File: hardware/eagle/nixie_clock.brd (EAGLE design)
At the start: 199.4 x 199.4 mm, 81 parts, among them IC1 74141N, IC10 7477N, IC11 74141N, IC12 7477N, IC13 74HCT259N, IC15 7477N, IC2 7477N, IC3 74141N, IC4 7477N, IC5 74141N, IC6 7477N, IC7 74141N, IC8 7477N, IC9 74141N, J1 RASPBERRYPI-40-PIN-GPIO, J1_180V 22-27-2021-02, J1_5V1 22-27-2021-02, J1_5V2 22-27-2021-02, K1 4052, SW1 ROTARTY_ENCODER

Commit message: Updated eagle project
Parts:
- removed SV1, SV11, SV13, SV3, SV5, SV7, SV9: (no value), con-lstb:MA06-1
- added J10, J4, J5, J6, J7, J8, J9: (no value), SparkFun-Connectors:1X08_ROUND
- added J2: (no value), SparkFun-Connectors:AVR_ICSP
- added J3: (no value), SparkFun-Connectors:1X04
- added SV17: (no value), con-lstb:MA09-2
- SV10, SV12, SV14, SV2, SV4, SV6, SV8: device con-lstb:MA05-1 -> SparkFun-Connectors:1X07
- moved R12 130.8 mm to (3.81, 36.8), turned to 270 degrees
- moved D1 128.1 mm to (90.2, 95.2), turned to 0 degrees
- moved IN-8-1 128.1 mm to (90.2, 95.2)
- moved SV14 122.3 mm to (97.8, 105.4)
- moved J1 13.1 mm to (181.6, 47.0)
- moved SV8 7.62 mm to (108.0, 27.9)
- moved SV4 7.62 mm to (62.2, 27.9)
- moved SV2 6.35 mm to (40.6, 27.9)
- moved SV12 6.35 mm to (154.9, 27.9)
- moved SV6 6.35 mm to (86.4, 27.9)
- moved SV10 5.08 mm to (132.1, 27.9)
- moved R5 2.54 mm to (124.5, 2.54), turned to 180 degrees
- moved R3 1.27 mm to (78.7, 2.54), turned to 180 degrees
- moved R6 1.27 mm to (147.3, 2.54), turned to 180 degrees
- moved R1 1.27 mm to (33.0, 2.54), turned to 180 degrees
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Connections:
- removed net 3.3V: J1.1, J1.17
- removed net 5V: J1.2, J1.4
- new net BLUE: J3.3, R11.2, SV10.7, SV12.7, SV2.7, SV4.7, SV6.7, SV8.7
- new net GREEN: J3.2, R10.2, SV10.6, SV12.6, SV2.6, SV4.6, SV6.6, SV8.6
- new net GROUND: C1.2, C10.2, C11.2, C12.2, C13.2, C16.2, C17.2, C2.2, C3.2, C4.2, C5.2, C6.2, C7.2, C8.2, C9.2, D2.A, IC1.5, IC10.4, IC11.5, IC12.4, IC13.13, IC13.16, IC15.4, IC2.4, IC3.5, IC4.4, IC5.5, IC6.4, IC7.5, IC8.4, IC9.5, J1_5V1.2, J3.4, K1.2, R12.2, R7.2, R8.1, SV10.5, SV12.5, SV16.1, SV2.5, SV4.5, SV6.5, SV8.5, ULN1.10
- new net N$145: J1.1, J2.1, SV17.1
- new net N$150: J7.8, R4.1
- new net N$153: J1.4, J2.4, SV17.4
- new net N$154: J1.3, J2.3, SV17.3
- new net N$155: J1.5, J2.5, SV17.5
- new net N$156: J1.6, J2.6, J2.9, SV17.6
- new net N$157: J1.27, SV17.7
- new net N$158: J1.28, SV17.9
- new net N$159: J1.8, SV17.8
- new net N$160: J1.10, SV17.10
- new net N$161: J1.19, SV17.11
- new net N$162: J1.21, SV17.13
- new net N$163: J1.23, SV17.15
- new net N$164: J4.8, R1.1
- new net N$165: J1.9, SV17.12
- new net N$166: J1.24, SV17.14
- new net N$167: J1.26, SV17.16
- new net N$168: J1.14, SV17.18
- new net N$169: J6.8, R3.1
- new net N$170: R1.2, R2.2, R3.2, R4.2, R5.2, R6.2
- new net N$171: J5.8, R2.1
- new net N$172: J1.2, J2.2, SV17.2
- new net RED: J3.1, R9.2, SV10.4, SV12.4, SV2.4, SV4.4, SV6.4, SV8.4
- net GND: no longer J1.14, J1.6, J1.9
- net N$1: now also IN-8-1.4, J10.1; no longer R2.1, SV4.3
- net N$10: now also IN-8-1.9, J10.6; no longer IC1.2, SV2.5
- net N$100: now also IC9.16, J8.7; no longer IC11.14, SV11.3
- net N$101: now also IC9.9, SV10.1; no longer IC11.11, SV11.4
- net N$102: now also IC9.8, SV10.2; no longer IC11.10, SV11.5
- net N$103: now also IC9.15, SV10.3; no longer IC11.1, SV11.6
- net N$104: now also J10.8; no longer SV14.3
- net N$105: now also IC11.11, J9.3; no longer IN-8-1.1, SV14.2
- net N$106: now also IC11.10, J9.4; no longer IN-8-1.2, SV14.1
- net N$107: now also IC11.1, J9.5; no longer IN-8-1.0, SV14.4
- net N$109: now also IC11.2, J9.6; no longer IN-8-1.9, SV14.5
- net N$11: now also IN-8-1.0, J10.7; no longer IC1.9, SV1.1
- net N$110: now also IC11.16, J9.7; no longer IN-8-1.8, SV13.6
- net N$111: now also IC11.9, SV12.1; no longer IN-8-1.7, SV13.5
- net N$112: now also IC11.8, SV12.2; no longer IN-8-1.6, SV13.4
- net N$113: now also IC11.15, SV12.3; no longer IN-8-1.5, SV13.3
- net N$114: now also J8.8, R5.1; no longer IN-8-1.4, SV13.2
- net N$115: now also J9.8, R6.1; no longer IN-8-1.3, SV13.1
- net N$12: now also IN-8-1.3, SV14.1; no longer IC1.13, SV1.2
- net N$13: now also IN-8-1.2, SV14.2; no longer IC1.14, SV1.3
- net N$14: now also IN-8-1.1, SV14.3; no longer IC1.11, SV1.4
- net N$15: now also D1.1, SV14.4; no longer IC1.10, SV1.5
- net N$152: now also J1.17, SV17.17; no longer C1.2, C10.2, C11.2, C12.2, C13.2, C16.2, C17.2, C2.2, C3.2, C4.2, C5.2, C6.2, C7.2, C8.2, C9.2, D2.A, IC1.5, IC10.4, IC11.5, IC12.4, IC13.13, IC13.16, IC15.4, IC2.4, IC3.5, IC4.4, IC5.5, IC6.4, IC7.5, IC8.4, IC9.5, J1_5V1.2, K1.2, R12.2, R7.2, R8.1, SV16.1, ULN1.10
- net N$18: now also IC1.13, J4.1; no longer IC3.8, SV4.1
- net N$19: now also IC1.14, J4.2; no longer IC3.15, SV4.2
- net N$20: now also D1.4, SV14.7; no longer IC3.16, SV4.4
- net N$21: now also D1.2, SV14.5; no longer IC3.2, SV4.5
- net N$22: now also D1.3, SV14.6; no longer IC3.9, SV3.1
- net N$23: now also IC1.11, J4.3; no longer IC3.13, SV3.2
- net N$24: now also IC1.10, J4.4; no longer IC3.14, SV3.3
- net N$25: now also IC1.1, J4.5; no longer IC3.11, SV3.4
- net N$26: now also IC1.2, J4.6; no longer IC3.10, SV3.5
- net N$27: now also IC1.9, SV2.1; no longer IC3.1, SV3.6
- net N$28: now also IC1.8, SV2.2; no longer R3.1, SV6.3
- net N$34: now also IC1.15, SV2.3; no longer IC5.8, SV6.1
- net N$35: now also IC1.16, J4.7; no longer IC5.15, SV6.2
- net N$36: now also IC3.13, J5.1; no longer IC5.16, SV6.4
- net N$37: now also IC3.14, J5.2; no longer IC5.2, SV6.5
- net N$38: now also IC3.11, J5.3; no longer IC5.9, SV5.1
- net N$39: now also IC3.10, J5.4; no longer IC5.13, SV5.2
- net N$40: now also IC3.1, J5.5; no longer IC5.14, SV5.3
- net N$41: now also IC3.2, J5.6; no longer IC5.11, SV5.4
- net N$42: now also IC3.16, J5.7; no longer IC5.10, SV5.5
- net N$43: now also IC3.9, SV4.1; no longer IC5.1, SV5.6
- net N$49: now also IC3.8, SV4.2; no longer R4.1, SV8.3
- net N$50: now also IC3.15, SV4.3; no longer IC7.8, SV8.1
- net N$51: now also IC5.13, J6.1; no longer IC7.15, SV8.2
- net N$52: now also IC5.14, J6.2; no longer IC7.16, SV8.4
- net N$53: now also IC5.11, J6.3; no longer IC7.2, SV8.5
- net N$54: now also IC5.10, J6.4; no longer IC7.9, SV7.1
- net N$55: now also IC5.1, J6.5; no longer IC7.13, SV7.2
- net N$56: now also IC5.2, J6.6; no longer IC7.14, SV7.3
- net N$57: now also IC5.16, J6.7; no longer IC7.11, SV7.4
- net N$58: now also IC5.9, SV6.1; no longer IC7.10, SV7.5
- net N$6: now also IN-8-1.5, J10.2; no longer R1.1, SV2.3
- net N$64: now also IC5.8, SV6.2; no longer IC7.1, SV7.6
- net N$65: now also IC5.15, SV6.3; no longer R5.1, SV10.3
- net N$66: now also IC7.13, J7.1; no longer IC9.8, SV10.1
- net N$67: now also IC7.14, J7.2; no longer IC9.15, SV10.2
- net N$68: now also IC7.11, J7.3; no longer IC9.16, SV10.4
- net N$69: now also IC7.10, J7.4; no longer IC9.2, SV10.5
- net N$7: now also IN-8-1.6, J10.3; no longer IC1.15, SV2.2
- net N$70: now also IC7.1, J7.5; no longer IC9.9, SV9.1
- net N$71: now also IC7.2, J7.6; no longer IC9.13, SV9.2
- net N$72: now also IC7.16, J7.7; no longer IC9.14, SV9.3
- net N$73: now also IC7.9, SV8.1; no longer IC1.1, SV1.6
- net N$79: now also IC7.8, SV8.2; no longer IC9.11, SV9.4
- net N$8: now also IN-8-1.7, J10.4; no longer IC1.8, SV2.1
- net N$80: now also IC7.15, SV8.3; no longer IC9.10, SV9.5
- net N$81: now also IC9.13, J8.1; no longer IC9.1, SV9.6
- net N$82: now also IC9.14, J8.2; no longer R6.1, SV12.3
- net N$83: now also IC9.11, J8.3; no longer IC11.8, SV12.1
- net N$84: now also IC9.10, J8.4; no longer IC11.15, SV12.2
- net N$85: now also IC9.1, J8.5; no longer IC11.16, SV12.4
- net N$86: now also IC9.2, J8.6; no longer IC11.2, SV12.5
- net N$87: now also IC11.13, J9.1; no longer IC11.9, SV11.1
- net N$88: now also IC11.14, J9.2; no longer IC11.13, SV11.2
- net N$9: now also IN-8-1.8, J10.5; no longer IC1.16, SV2.4
- net VCC: no longer R1.2, R2.2, R3.2, R4.2, R5.2, R6.2
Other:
- board size 199.4 x 199.4 mm -> 188 x 200.7 mm

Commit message: Updated eagle project
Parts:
- added J11: (no value), SparkFun-Connectors:1X03
- SV15, SV16: device con-lstb:MA05-1 -> SparkFun-Connectors:1X05
- moved SV17 53.5 mm to (170.2, 61.0), turned to 90 degrees
- moved J3 15.5 mm to (171.4, 44.5), turned to 270 degrees
- moved J2 8.98 mm to (166.4, 29.2)
- moved SV15 5.24 mm to (59.7, 83.8)
- moved C18 4.02 mm to (57.1, 64.8)
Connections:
- removed net GROUND: C1.2, C10.2, C11.2, C12.2, C13.2, C16.2, C17.2, C2.2, C3.2, C4.2, C5.2, C6.2, C7.2, C8.2, C9.2, D2.A, IC1.5, IC10.4, IC11.5, IC12.4, IC13.13, IC13.16, IC15.4, IC2.4, IC3.5, IC4.4, IC5.5, IC6.4, IC7.5, IC8.4, IC9.5, J1_5V1.2, J3.4, K1.2, R12.2, R7.2, R8.1, SV10.5, SV12.5, SV16.1, SV2.5, SV4.5, SV6.5, SV8.5, ULN1.10
- new net 5V: C1.2, C10.2, C11.2, C12.2, C13.2, C16.2, C17.2, C2.2, C3.2, C4.2, C5.2, C6.2, C7.2, C8.2, C9.2, D2.A, IC1.5, IC10.4, IC11.5, IC12.4, IC13.13, IC13.16, IC15.4, IC2.4, IC3.5, IC4.4, IC5.5, IC6.4, IC7.5, IC8.4, IC9.5, J11.2, J1_5V1.2, J3.4, K1.2, R12.2, R7.2, R8.1, SV10.5, SV12.5, SV16.1, SV2.5, SV4.5, SV6.5, SV8.5, ULN1.10
- new net N$173: J1.36, J11.3
- net GND: now also J11.1
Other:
- board text added: "5V"
- board text added: "BLUE"
- board text added: "GREEN"
- board text added: "RED"

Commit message: freecad model updated
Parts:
- J11: device SparkFun-Connectors:1X03 -> con-amp-quick:03P
- J3: device SparkFun-Connectors:1X04 -> con-amp-quick:04P
- SV16: device SparkFun-Connectors:1X05 -> con-amp-quick:05P
- moved F1 302.6 mm to (306.1, 33.0)
- moved F2 301.0 mm to (320.0, 33.0), turned to 90 degrees
- moved LSP2 277.9 mm to (261.6, 30.5)
- moved LSP1 271.9 mm to (261.6, 21.6)
- moved B1 264.5 mm to (313.7, 81.3)
- moved KK1 264.5 mm to (313.7, 85.1)
- moved C15 262.3 mm to (320.0, 58.4)
- moved TR1 261.5 mm to (278.1, 66.0)
- moved C14 261.1 mm to (306.1, 58.4)
- moved IC14 257.0 mm to (306.1, 72.4)
- moved J1_5V2 232.1 mm to (292.1, 34.3)
- moved R12 229.6 mm to (232.4, 15.2), turned to 90 degrees
- moved J1_180V 214.5 mm to (223.5, 45.7), turned to 0 degrees
- moved D2 214.0 mm to (223.5, 7.62), turned to 0 degrees
- moved K1 211.7 mm to (223.5, 16.5), turned to 90 degrees
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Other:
- board size 188 x 200.7 mm -> 330.2 x 142.2 mm
- board text added: "3.3V"
- board text added: "CE0"
- board text added: "CE1"
- board text added: "GND"
- board text added: "ID_SC"
- board text added: "ID_SD"
- board text added: "MISO"
- board text added: "MOSI"
- board text added: "PIR"
- board text added: "RTC With BAT"
- board text added: "RX"
- board text added: "SCL"
- board text added: "SCLK"
- board text added: "SDA"
- board text added: "SIA"
- board text added: "SIB"
- board text added: "SW"
- board text added: "TX"
- board text added: "VCC"

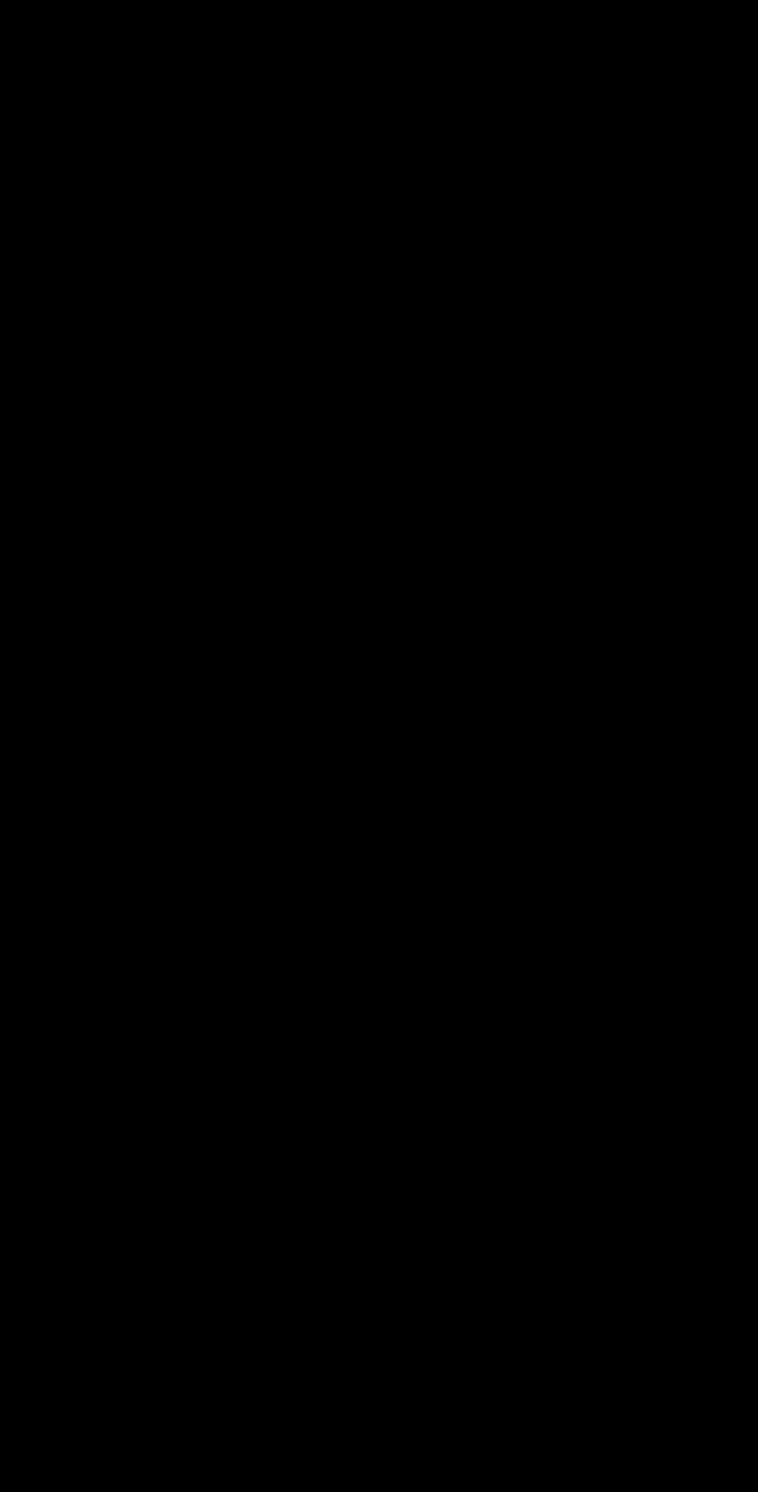
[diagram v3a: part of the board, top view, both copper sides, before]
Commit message: Fixed problem related with the pcb
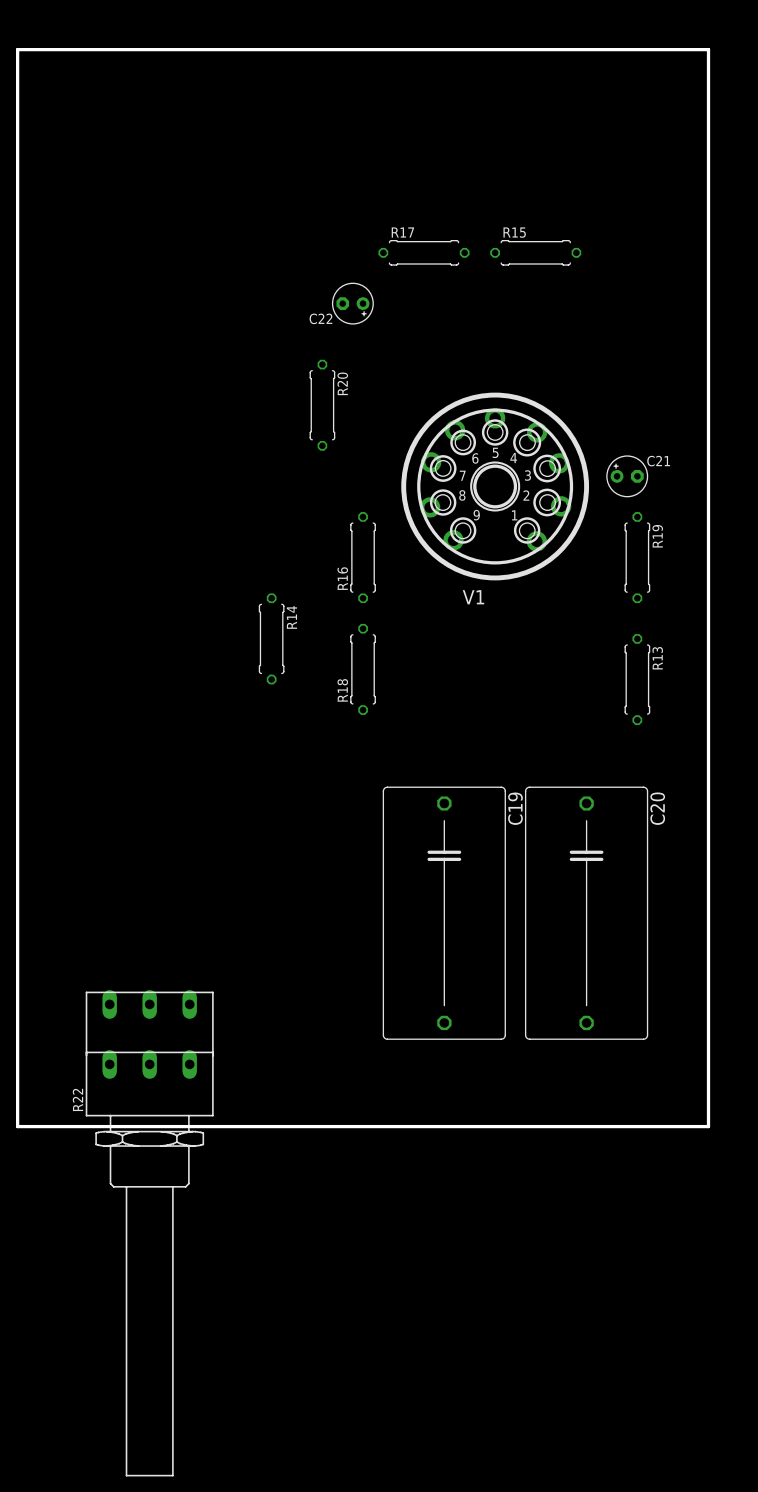
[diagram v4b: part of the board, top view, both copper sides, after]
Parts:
- added C19: 0.47uF 300V, resistor:C275-154X316
- added C20: 0,47uF 300V, resistor:C275-154X316
- added C21, C22: (no value), resistor:E2,5-5
- added R13, R14: 100k, resistor:0309/10
- added R15, R16: 10k, resistor:0309/10
- added R17, R18: 470k, resistor:0309/10
- added R19, R20: 1k2, resistor:0309/10
- added R22: PC16D, piher:PC16D
- added V1: (no value), Tubes:NOVAL
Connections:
- removed net N$145: J1.1, J2.1, SV17.1
- new net N$174: R15.1, R17.2
- new net N$175: R16.1, R18.2
- new net N$176: R15.2, V1.2
- new net N$177: C20.1, R13.1, V1.1
- new net N$178: C19.1, R14.1, V1.6
- new net N$179: R16.2, V1.7
- new net N$180: C22.+, C22.-, R20.1, R20.2, V1.8
- new net N$181: C21.+, R19.2, V1.3
- new net N$182: J11.2, R8.1, SV16.1
- new net N$184: C20.2, R22.1A
- new net N$185: C19.2, R22.2A
- net 5V: no longer J11.2, R8.1, SV16.1
- net GND: now also C21.-, R17.1, R18.1, R19.1, R22.1E, R22.2E
- net N$130: now also J1.1, J2.1, SV17.1
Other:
- board size 330.2 x 142.2 mm -> 330.2 x 295.9 mm
